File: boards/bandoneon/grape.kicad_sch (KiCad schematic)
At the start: 9 parts, among them U1 MCP3008

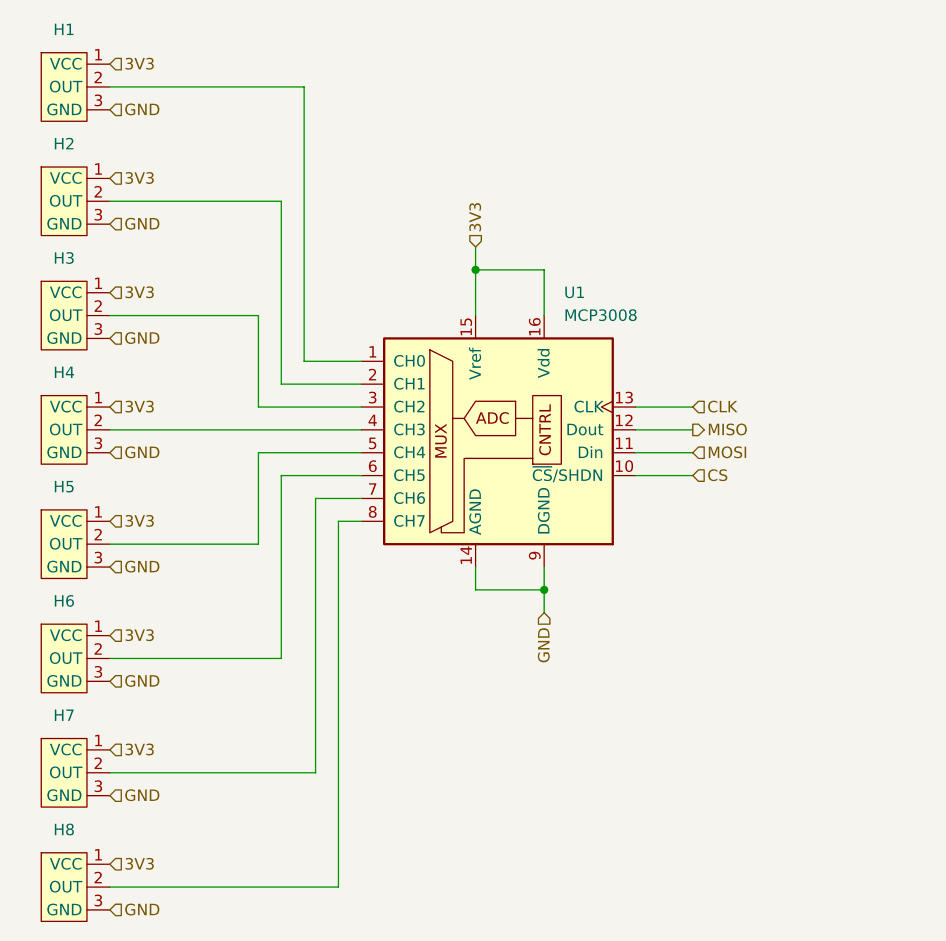
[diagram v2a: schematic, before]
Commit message: Fix component side
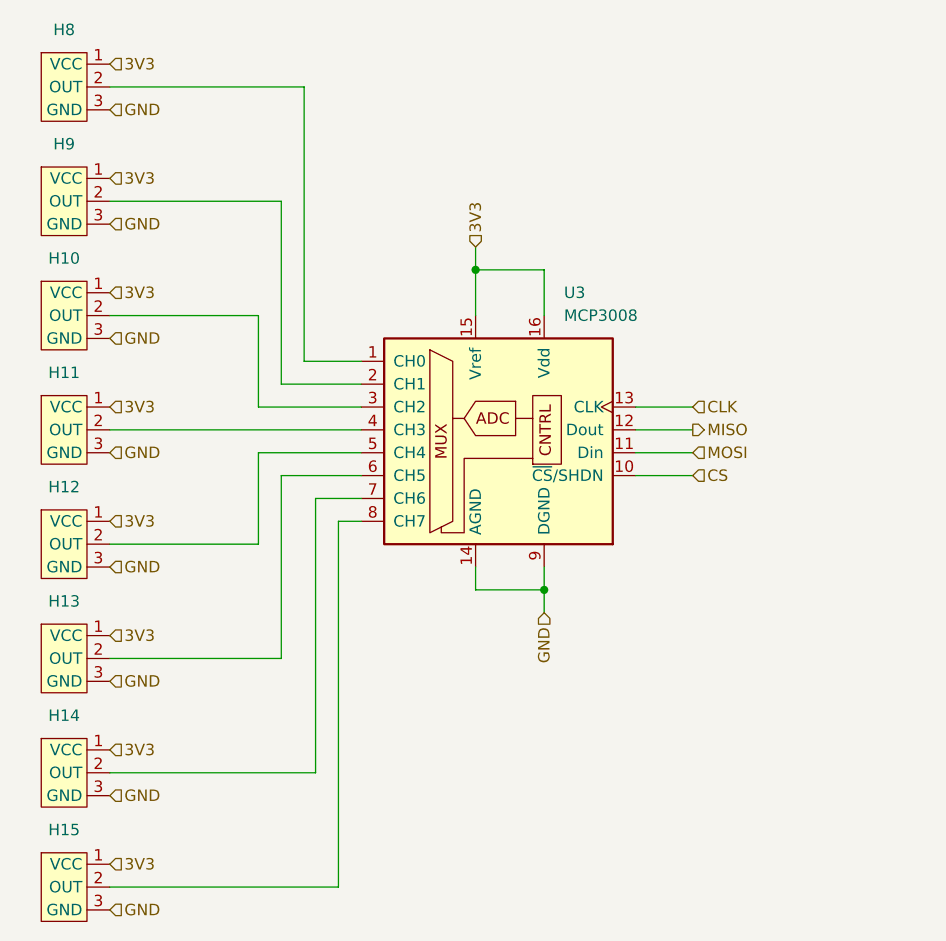
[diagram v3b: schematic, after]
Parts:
- renumbered H3 to H10, H4 to H11, H5 to H12, H6 to H13, H7 to H14, H8 to H15, H1 to H8, H2 to H9, U1 to U3

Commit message: Add models and ground plane
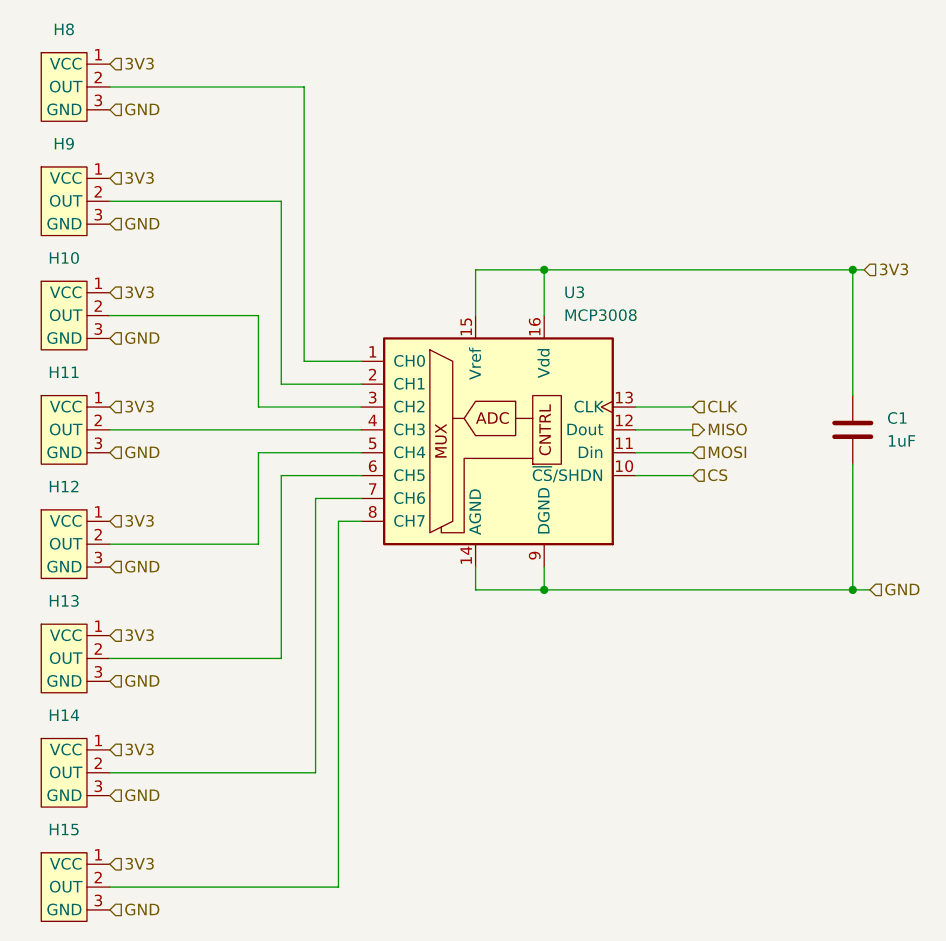
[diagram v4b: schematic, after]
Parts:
- added C1: 1uF, symbol Device:C
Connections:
- net 3V3: now also C1.1
- net GND: now also C1.2
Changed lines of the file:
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@@
 (kicad_sch (version 20230121) (generator eeschema)
   (paper "A5")
+  (junction (at 127 85.09) (diameter 0) (color 0 0 0 0)
+  )
   (junction (at 92.71 85.09) (diameter 0) (color 0 0 0 0)
   )
-  (junction (at 85.09 49.53) (diameter 0) (color 0 0 0 0)
+  (junction (at 92.71 49.53) (diameter 0) (color 0 0 0 0)
+  )
+  (junction (at 127 49.53) (diameter 0) (color 0 0 0 0)
   )
   (wire (pts (xy 60.96 80.01) (xy 60.96 69.85))
@@
     (stroke (width 0) (type default))
   )
+  (wire (pts (xy 127 71.12) (xy 127 85.09))
+    (stroke (width 0) (type default))
+  )
   (wire (pts (xy 102.87 64.77) (xy 109.22 64.77))
     (stroke (width 0) (type default))
@@
     (stroke (width 0) (type default))
   )
+  (wire (pts (xy 92.71 85.09) (xy 127 85.09))
+    (stroke (width 0) (type default))
+  )
   (wire (pts (xy 63.5 92.71) (xy 63.5 72.39))
     (stroke (width 0) (type default))
@@
     (stroke (width 0) (type default))
   )
-  (wire (pts (xy 92.71 85.09) (xy 92.71 87.63))
-    (stroke (width 0) (type default))
-  )
   (wire (pts (xy 92.71 54.61) (xy 92.71 49.53))
     (stroke (width 0) (type default))
   )
-  (wire (pts (xy 85.09 46.99) (xy 85.09 49.53))
+  (wire (pts (xy 127 49.53) (xy 92.71 49.53))
+    (stroke (width 0) (type default))
+  )
+  (wire (pts (xy 128.27 49.53) (xy 127 49.53))
     (stroke (width 0) (type default))
   )
@@
     (stroke (width 0) (type default))
   )
+  (wire (pts (xy 127 49.53) (xy 127 63.5))
+    (stroke (width 0) (type default))
+  )
   (wire (pts (xy 85.09 82.55) (xy 85.09 85.09))
     (stroke (width 0) (type default))
@@
     (stroke (width 0) (type default))
   )
+  (wire (pts (xy 127 85.09) (xy 128.905 85.09))
+    (stroke (width 0) (type default))
+  )
   (wire (pts (xy 92.71 82.55) (xy 92.71 85.09))
     (stroke (width 0) (type default))
@@
     (effects (font (size 1.27 1.27)) (justify left))
   )
-  (hierarchical_label "GND" (shape input) (at 92.71 87.63 270) (fields_autoplaced)
-    (effects (font (size 1.27 1.27)) (justify right))
+  (hierarchical_label "GND" (shape input) (at 128.905 85.09 0) (fields_autoplaced)
+    (effects (font (size 1.27 1.27)) (justify left))
   )
   (hierarchical_label "GND" (shape input) (at 44.45 107.95 0) (fields_autoplaced)
@@
     (effects (font (size 1.27 1.27)) (justify left))
   )
-  (hierarchical_label "3V3" (shape input) (at 85.09 46.99 90) (fields_autoplaced)
+  (hierarchical_label "3V3" (shape input) (at 128.27 49.53 0) (fields_autoplaced)
     (effects (font (size 1.27 1.27)) (justify left))
   )
@@
     (effects (font (size 1.27 1.27)) (justify left))
   )
+  (symbol (lib_id "Device:C") (at 127 67.31 0) (unit 1)
+    (in_bom yes) (on_board yes) (dnp no) (fields_autoplaced)
+    (property "Reference" "C1" (at 130.81 66.04 0)
+      (effects (font (size 1.27 1.27)) (justify left))
+    )
+    (property "Value" "1uF" (at 130.81 68.58 0)
+      (effects (font (size 1.27 1.27)) (justify left))
+    )
+    (property "Footprint" "" (at 127.9652 71.12 0)
+      (effects (font (size 1.27 1.27)) hide)
+    )
+    (property "Datasheet" "~" (at 127 67.31 0)
+      (effects (font (size 1.27 1.27)) hide)
+    )
+    (pin "2")
+    (pin "1")
+    (instances
+      (project "bandoneon"
+        (path "/3628cda3-bad1-4014-a851-91434ca52087/281879d1-17d5-476a-8152-9052381f6dcd"
+          (reference "C1") (unit 1)
+        )
+        (path "/3628cda3-bad1-4014-a851-91434ca52087/c1331607-7beb-4328-8168-0ef2d7f0c3a8"
+          (reference "C2") (unit 1)
+        )
+        (path "/3628cda3-bad1-4014-a851-91434ca52087/37f02563-9dad-45dc-aef9-616762245c01"
+          (reference "C3") (unit 1)
+        )
+        (path "/3628cda3-bad1-4014-a851-91434ca52087/cbc0efbc-019d-423d-9c3b-01d851bb921b"
+          (reference "C4") (unit 1)
+        )
+        (path "/3628cda3-bad1-4014-a851-91434ca52087/e5cf261c-2dfa-405f-b40f-26adaf491a2b"
+          (reference "C5") (unit 1)
+        )
+        (path "/3628cda3-bad1-4014-a851-91434ca52087/0a8ae72f-05c4-432a-8f4c-17acfbc27e43"
+          (reference "C6") (unit 1)
+        )
+        (path "/3628cda3-bad1-4014-a851-91434ca52087/01fa17a4-91ce-4047-8069-8dd63b35a268"
+          (reference "C7") (unit 1)
+        )
+        (path "/3628cda3-bad1-4014-a851-91434ca52087/59d98d07-b4e7-4311-9e60-029d7a5b8da0"
+          (reference "C8") (unit 1)
+        )
+      )
+    )
+  )
   (symbol (lib_id "Library:SS39ET") (at 39.37 105.41 0) (unit 1)

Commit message: Complete manual wire
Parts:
- C1: footprint (none) -> Capacitor_SMD:C_0402_1005Metric
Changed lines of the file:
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@@
       (effects (font (size 1.27 1.27)) (justify left))
     )
-    (property "Footprint" "" (at 127.9652 71.12 0)
+    (property "Footprint" "Capacitor_SMD:C_0402_1005Metric" (at 127.9652 71.12 0)
       (effects (font (size 1.27 1.27)) hide)
     )

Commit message: Add esd protection
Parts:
- U3: LCSC (none) -> C1520159; Vendor (none) -> https://jlcpcb.com/partdetail/MicrochipTech-MCP3008_ISL/C15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
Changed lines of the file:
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@@
+      (effects (font (size 1.27 1.27)) hide)
+    )
+    (property "LCSC" "C1520159" (at 87.63 67.31 0)
+      (effects (font (size 1.27 1.27)) hide)
+    )
+    (property "Vendor" "https://jlcpcb.com/partdetail/MicrochipTech-MCP3008_ISL/C1520159" (at 87.63 67.31 0)
       (effects (font (size 1.27 1.27)) hide)
     )

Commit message: Gerber and bom export
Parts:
- C1: LCSC Part (none) -> C52923
- H10, H11, H12, H13, H14, H15, H8, H9: value ~ -> SS39ET; footprint Library:SS39ET -> Library:SOT-23_SS39ET; LCSC Part (none) -> C126669
- U3: footprint Library:MCP3008T-I_SL -> Library:SOIC-16_MCP3008T-I_SL; LCSC C1520159 -> (none); LCSC Part (none) -> C1520159
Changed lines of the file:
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@@
       (effects (font (size 1.27 1.27)) hide)
     )
-    (property "Datasheet" "~" (at 127 67.31 0)
+    (property "Datasheet" "https://jlcpcb.com/partdetail/53938-CL05A105KA5NQNC/C52923" (at 127 67.31 0)
+      (effects (font (size 1.27 1.27)) hide)
+    )
+    (property "LCSC Part" "C52923" (at 127 67.31 0)
       (effects (font (size 1.27 1.27)) hide)
     )
@@
       (effects (font (size 1.27 1.27)))
     )
-    (property "Value" "~" (at 40.64 104.14 0)
-      (effects (font (size 1.27 1.27)))
-    )
-    (property "Footprint" "Library:SS39ET" (at 40.64 104.14 0)
-      (effects (font (size 1.27 1.27)) hide)
-    )
-    (property "Datasheet" "" (at 40.64 104.14 0)
+    (property "Value" "SS39ET" (at 35.56 105.41 90)
+      (effects (font (size 1.27 1.27)))
+    )
+    (property "Footprint" "Library:SOT-23_SS39ET" (at 40.64 110.49 0)
+      (effects (font (size 1.27 1.27)) hide)
+    )
+    (property "Datasheet" "https://jlcpcb.com/partdetail/Honeywell-SS39ET/C126669" (at 40.64 114.3 0)
+      (effects (font (size 1.27 1.27)) hide)
+    )
+    (property "LCSC Part" "C126669" (at 39.37 112.522 0)
       (effects (font (size 1.27 1.27)) hide)
     )
@@
       (effects (font (size 1.27 1.27)))
     )
-    (property "Value" "~" (at 40.64 53.34 0)
-      (effects (font (size 1.27 1.27)))
-    )
-    (property "Footprint" "Library:SS39ET" (at 40.64 53.34 0)
-      (effects (font (size 1.27 1.27)) hide)
-    )
-    (property "Datasheet" "" (at 40.64 53.34 0)
+    (property "Value" "SS39ET" (at 35.56 54.61 90)
+      (effects (font (size 1.27 1.27)))
+    )
+    (property "Footprint" "Library:SOT-23_SS39ET" (at 40.64 59.69 0)
+      (effects (font (size 1.27 1.27)) hide)
+    )
+    (property "Datasheet" "https://jlcpcb.com/partdetail/Honeywell-SS39ET/C126669" (at 40.64 63.5 0)
+      (effects (font (size 1.27 1.27)) hide)
+    )
+    (property "LCSC Part" "C126669" (at 39.37 61.722 0)
       (effects (font (size 1.27 1.27)) hide)
     )
@@
       (effects (font (size 1.27 1.27)) (justify left))
     )
-    (property "Footprint" "Library:MCP3008T-I_SL" (at 90.17 64.77 0)
+    (property "Footprint" "Library:SOIC-16_MCP3008T-I_SL" (at 90.17 64.77 0)
       (effects (font (size 1.27 1.27)) hide)
     )
@@
       (effects (font (size 1.27 1.27)) hide)
     )
-    (property "LCSC" "C1520159" (at 87.63 67.31 0)
+    (property "LCSC Part" "C1520159" (at 87.63 67.31 0)
       (effects (font (size 1.27 1.27)) hide)
     )
@@
       (effects (font (size 1.27 1.27)))
     )
-    (property "Value" "~" (at 40.64 40.64 0)
-      (effects (font (size 1.27 1.27)))
-    )
-    (property "Footprint" "Library:SS39ET" (at 40.64 40.64 0)
-      (effects (font (size 1.27 1.27)) hide)
-    )
-    (property "Datasheet" "" (at 40.64 40.64 0)
+    (property "Value" "SS39ET" (at 35.56 41.91 90)
+      (effects (font (size 1.27 1.27)))
+    )
+    (property "Footprint" "Library:SOT-23_SS39ET" (at 40.64 46.99 0)
+      (effects (font (size 1.27 1.27)) hide)
+    )
+    (property "Datasheet" "https://jlcpcb.com/partdetail/Honeywell-SS39ET/C126669" (at 40.64 50.8 0)
+      (effects (font (size 1.27 1.27)) hide)
+    )
+    (property "LCSC Part" "C126669" (at 39.37 49.022 0)
       (effects (font (size 1.27 1.27)) hide)
     )
@@
       (effects (font (size 1.27 1.27)))
     )
-    (property "Value" "~" (at 40.64 27.94 0)
-      (effects (font (size 1.27 1.27)))
-    )
-    (property "Footprint" "Library:SS39ET" (at 40.64 27.94 0)
-      (effects (font (size 1.27 1.27)) hide)
-    )
-    (property "Datasheet" "" (at 40.64 27.94 0)
+    (property "Value" "SS39ET" (at 35.56 29.21 90)
+      (effects (font (size 1.27 1.27)))
+    )
+    (property "Footprint" "Library:SOT-23_SS39ET" (at 40.64 34.29 0)
+      (effects (font (size 1.27 1.27)) hide)
+    )
+    (property "Datasheet" "https://jlcpcb.com/partdetail/Honeywell-SS39ET/C126669" (at 40.64 38.1 0)
+      (effects (font (size 1.27 1.27)) hide)
+    )
+    (property "LCSC Part" "C126669" (at 39.37 36.322 0)
       (effects (font (size 1.27 1.27)) hide)
     )
@@
       (effects (font (size 1.27 1.27)))
     )
-    (property "Value" "~" (at 40.64 91.44 0)
-      (effects (font (size 1.27 1.27)))
-    )
-    (property "Footprint" "Library:SS39ET" (at 40.64 91.44 0)
-      (effects (font (size 1.27 1.27)) hide)
-    )
-    (property "Datasheet" "" (at 40.64 91.44 0)
+    (property "Value" "SS39ET" (at 35.56 92.71 90)
+      (effects (font (size 1.27 1.27)))
+    )
+    (property "Footprint" "Library:SOT-23_SS39ET" (at 40.64 97.79 0)
+      (effects (font (size 1.27 1.27)) hide)
+    )
+    (property "Datasheet" "https://jlcpcb.com/partdetail/Honeywell-SS39ET/C126669" (at 40.64 101.6 0)
+      (effects (font (size 1.27 1.27)) hide)
+    )
+    (property "LCSC Part" "C126669" (at 39.37 99.822 0)
       (effects (font (size 1.27 1.27)) hide)
     )
@@
       (effects (font (size 1.27 1.27)))
     )
-    (property "Value" "~" (at 40.64 116.84 0)
-      (effects (font (size 1.27 1.27)))
-    )
-    (property "Footprint" "Library:SS39ET" (at 40.64 116.84 0)
-      (effects (font (size 1.27 1.27)) hide)
-    )
-    (property "Datasheet" "" (at 40.64 116.84 0)
+    (property "Value" "SS39ET" (at 35.56 118.11 90)
+      (effects (font (size 1.27 1.27)))
+    )
+    (property "Footprint" "Library:SOT-23_SS39ET" (at 40.64 123.19 0)
+      (effects (font (size 1.27 1.27)) hide)
+    )
+    (property "Datasheet" "https://jlcpcb.com/partdetail/Honeywell-SS39ET/C126669" (at 40.64 127 0)
+      (effects (font (size 1.27 1.27)) hide)
+    )
+    (property "LCSC Part" "C126669" (at 39.37 125.222 0)
       (effects (font (size 1.27 1.27)) hide)
     )
@@
       (effects (font (size 1.27 1.27)))
     )
-    (property "Value" "~" (at 40.64 78.74 0)
-      (effects (font (size 1.27 1.27)))
-    )
-    (property "Footprint" "Library:SS39ET" (at 40.64 78.74 0)
-      (effects (font (size 1.27 1.27)) hide)
-    )
-    (property "Datasheet" "" (at 40.64 78.74 0)
+    (property "Value" "SS39ET" (at 35.56 80.01 90)
+      (effects (font (size 1.27 1.27)))
+    )
+    (property "Footprint" "Library:SOT-23_SS39ET" (at 40.64 85.09 0)
+      (effects (font (size 1.27 1.27)) hide)
+    )
+    (property "Datasheet" "https://jlcpcb.com/partdetail/Honeywell-SS39ET/C126669" (at 40.64 88.9 0)
+      (effects (font (size 1.27 1.27)) hide)
+    )
+    (property "LCSC Part" "C126669" (at 39.37 87.122 0)
       (effects (font (size 1.27 1.27)) hide)
     )
@@
       (effects (font (size 1.27 1.27)))
     )
-    (property "Value" "~" (at 40.64 66.04 0)
-      (effects (font (size 1.27 1.27)))
-    )
-    (property "Footprint" "Library:SS39ET" (at 40.64 66.04 0)
-      (effects (font (size 1.27 1.27)) hide)
-    )
-    (property "Datasheet" "" (at 40.64 66.04 0)
-      (effects (font (size 1.27 1.27)) hide)
-    )
+    (property "Value" "SS39ET" (at 35.56 67.31 90)
+      (effects (font (size 1.27 1.27)))
+    )
+    (property "Footprint" "Library:SOT-23_SS39ET" (at 40.64 72.39 0)
+      (effects (font (size 1.27 1.27)) hide)
+    )
+    (property "Datasheet" "https://jlcpcb.com/partdetail/Honeywell-SS39ET/C126669" (at 40.64 76.2 0)
+      (effects (font (size 1.27 1.27)) hide)
+    )
+    (property "LCSC Part" "C126669" (at 39.37 74.422 0)
+      (effects (font (size 1.27 1.27)) hide)
+    )
